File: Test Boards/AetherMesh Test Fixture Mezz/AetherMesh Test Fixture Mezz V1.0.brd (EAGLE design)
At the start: 71.2 x 57.5 mm, 8 parts, among them J1 POWER_JACKEJ508A, M1 AETHERMESH_MODULEMEZZ-HOLES

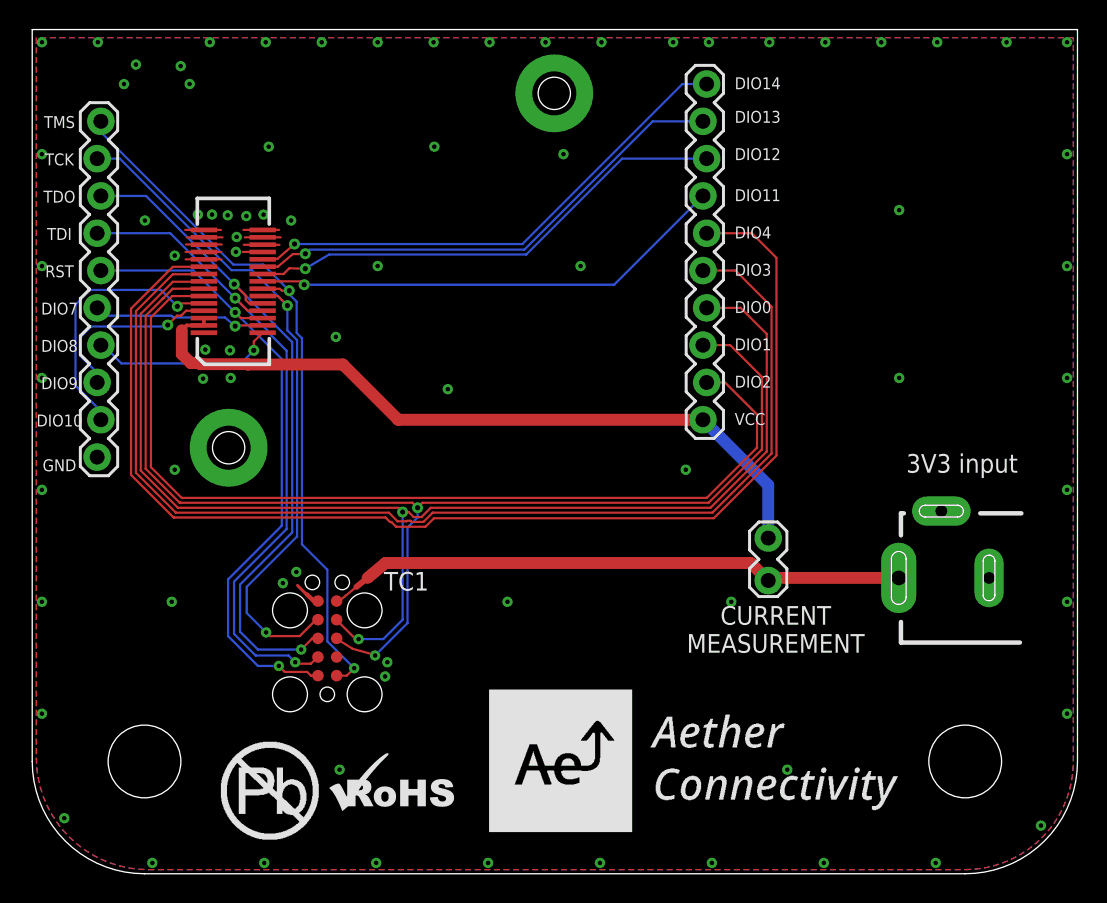
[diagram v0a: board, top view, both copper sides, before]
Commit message: Updated reference designs and test boards with latest XDS programmer tag connect header
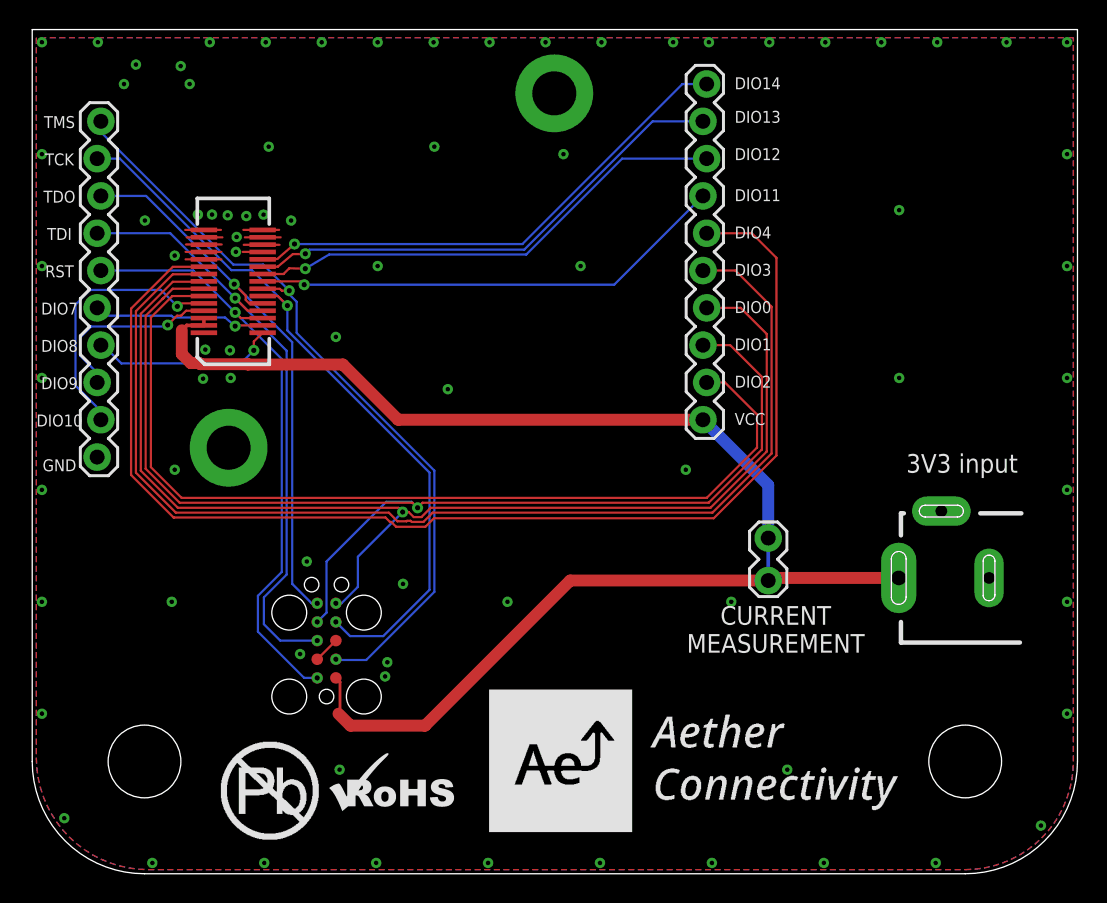
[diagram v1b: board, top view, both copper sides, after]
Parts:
- removed TC1: TC2050-IDC, TagConnect:TC2050-IDC
- added TC3: TC2050-IDC, TagConnect:TC2050-IDC
- M1: value AETHERMESH_MODULEMEZZ-HOLES -> AETHERMESH_MODULEMEZZ-NOHOLES; device AetherConnectivity:AETHERMESH_MEZZ_MOUNT_HOLES -> AetherConnectivity:AETHERMESH_MEZZ_MOUNT_NOHOLES
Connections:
- net DIO0-RX: now also TC3.5; no longer TC1.7
- net DIO1-TX: now also TC3.7; no longer TC1.5
- net GND: now also TC3.3, TC3.9; no longer TC1.10, TC1.3
- net RESET: now also TC3.10; no longer TC1.2
- net TCK: now also TC3.4; no longer TC1.8
- net TDI: now also TC3.8; no longer TC1.4
- net TDO: now also TC3.6; no longer TC1.6
- net TMS: now also TC3.2; no longer TC1.1
- net VCC: now also TC3.1; no longer TC1.9
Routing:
- net TDO: track 47.1 -> 38.5 mm
- net VCC: track 39.8 -> 48.2 mm
- net DIO0-RX: track 87.4 -> 82.8 mm
- net TMS: track 48.9 -> 53.2 mm
- net TDI: track 46.0 -> 41.8 mm
- net RESET: track 44.5 -> 41.4 mm
- net TCK: track 47.6 -> 50.6 mm
- net DIO1-TX: track 84.0 -> 82.2 mm
- net GND: vias 78 -> 79
